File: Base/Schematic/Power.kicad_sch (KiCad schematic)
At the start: 13 parts, among them U2 TPS560430XDBV

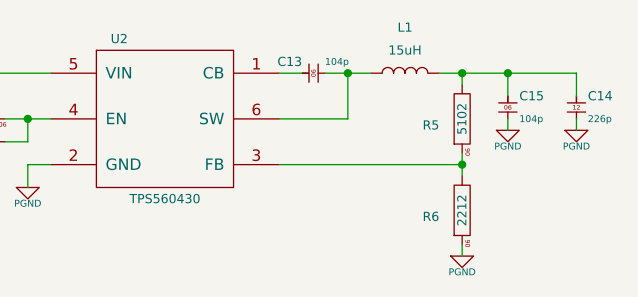
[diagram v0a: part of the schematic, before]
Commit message: [BOM 문서 테스트] - Libreoffice로 BOM 문서 출력 테스트 - 회로도에 CAN transceiver 추가
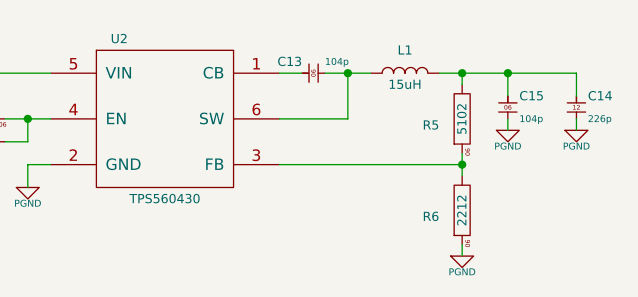
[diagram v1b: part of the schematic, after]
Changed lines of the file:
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@@
 		(on_board yes)
 		(dnp no)
-		(fields_autoplaced yes)
 		(property "Reference" "L1"
-			(at 176.53 92.71 0)
+			(at 176.53 95.25 0)
 			(effects
 				(font
@@
 		)
 		(property "#Value" "15uH"
-			(at 176.53 95.25 0)
+			(at 176.53 99.06 0)
 			(effects
 				(font

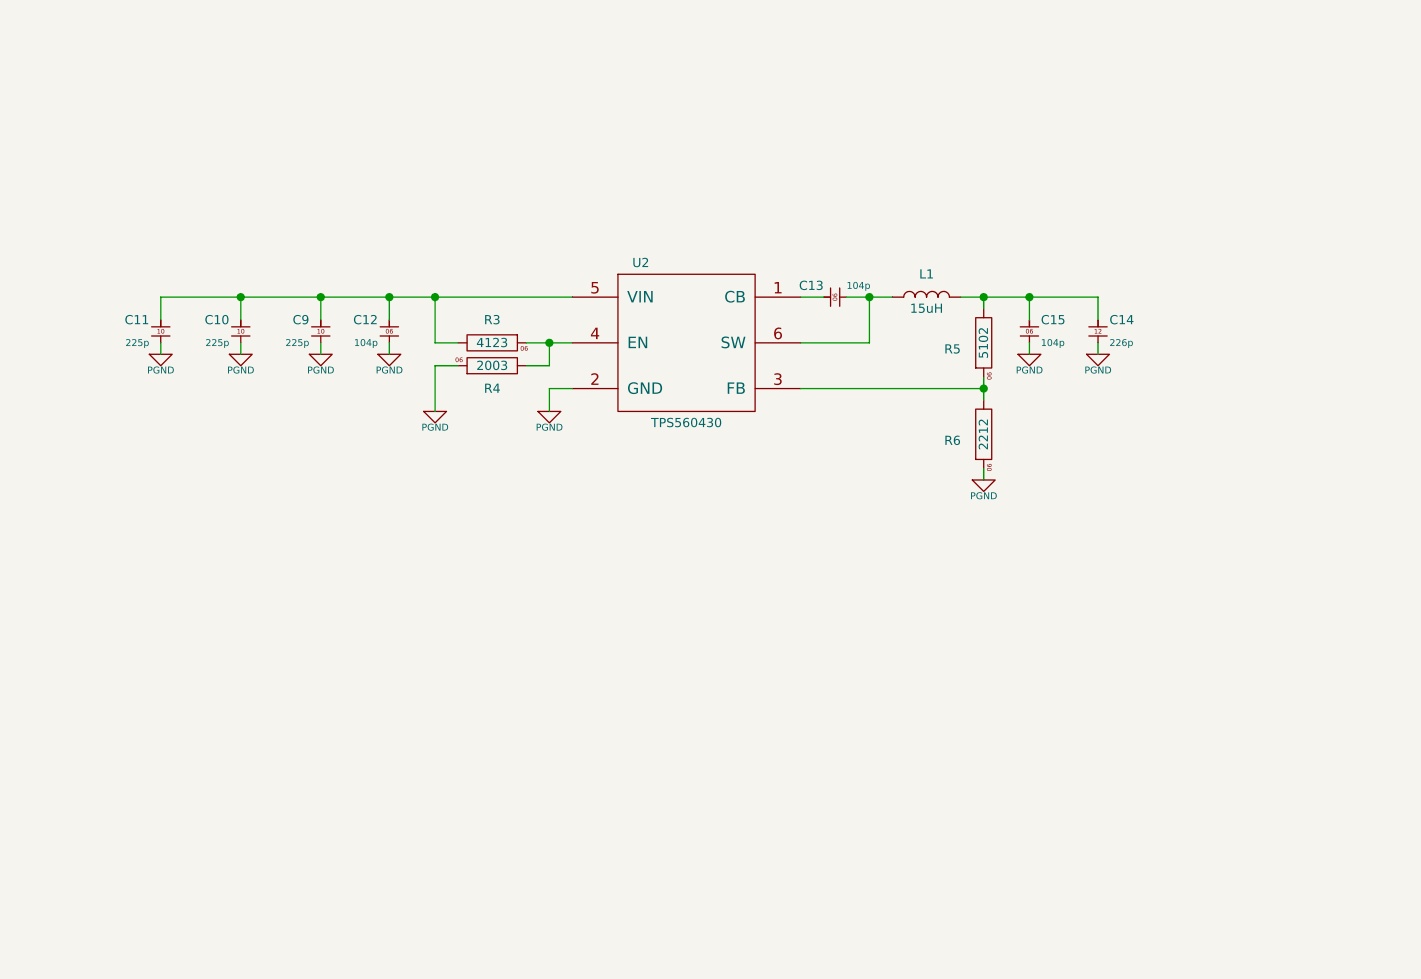
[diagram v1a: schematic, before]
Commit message: [Base 회로도 업데이트] - 5V 전원 추가 - 3.3V, 5V 회로도 보완
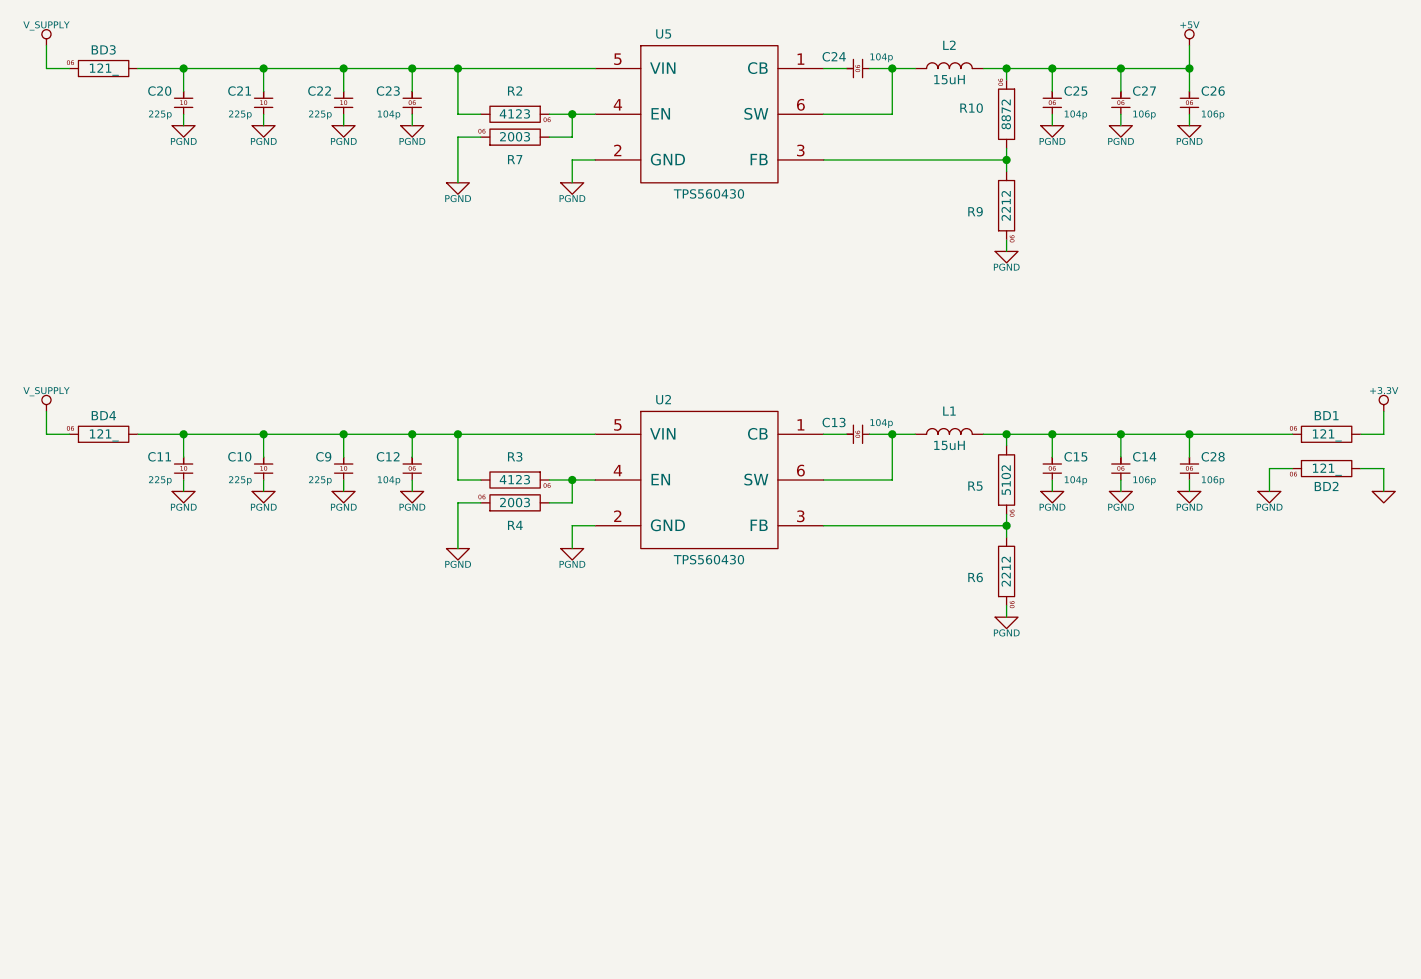
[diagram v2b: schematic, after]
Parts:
- removed C14: 1206B226K100, SMC:1206, symbol Capacitor_MLCC:1206B226K100
- added BD1, BD2, BD3, BD4: BLM18KG121TN1D, SML:0603, symbol BEAD:BLM18KG121TN1D
- added C14, C26, C27, C28: 0603X106K100, SMC:0603, symbol Capacitor_MLCC:0603X106K100
- added C20, C21, C22: 1210B225K101, SMC:1210, symbol Capacitor_MLCC:1210B225K101
- added C23, C24, C25: 0603B104K500, SMC:0603, symbol Capacitor_MLCC:0603B104K500
- added L2: SWPA5040S150MT, Sunlord:SWPA5040S, symbol Inductor_Power:SWPA5040S150MT
- added R10: WR06X8872FTL, SMR:0603, symbol Resistor:WR06X8872FTL
- added R2: WR06X4123FTL, SMR:0603, symbol Resistor:WR06X4123FTL
- added R7: WR06X2003FTL, SMR:0603, symbol Resistor:WR06X2003FTL
- added R9: WR06X2212FTL, SMR:0603, symbol Resistor:WR06X2212FTL
- added U5: TPS560430XDBV, TI:DBV0006A, symbol Power_DCDC:TPS560430XDBV
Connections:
- net PGND: now also BD2.1, C14.1, C20.1, C21.1, C22.1, C23.1, C25.1, C26.1, C27.1, C28.1, R7.1, R9.1, U5.2 (GND)
- net at C15.2, L1.2, R5.2: now also BD1.1, C14.2, C28.2
- net at C10.2, C11.2, C12.2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: now also BD4.2
- new net: BD3.2, C20.2, C21.2, C22.2, C23.2, R2.2, U5.5 (VIN)
- new net: R10.2, R9.2, U5.3 (FB)
- new net: C24.1, L2.1, U5.6 (SW)
- new net: C24.2, U5.1 (CB)
- new net: R2.1, R7.2, U5.4 (EN)
- new net +3.3V: BD1.2
- new net +5V: C25.2, C26.2, C27.2, L2.2, R10.1
- new net GND: BD2.2
- new net V_SUPPLY: BD3.1, BD4.1
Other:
- moved on the sheet: C10, C11, C12, C13, C15, C9, L1, R3, R4, R5, R6, U2

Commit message: [Base PCB 업데이트] - PCB 외곽선과 볼트 위치 설정
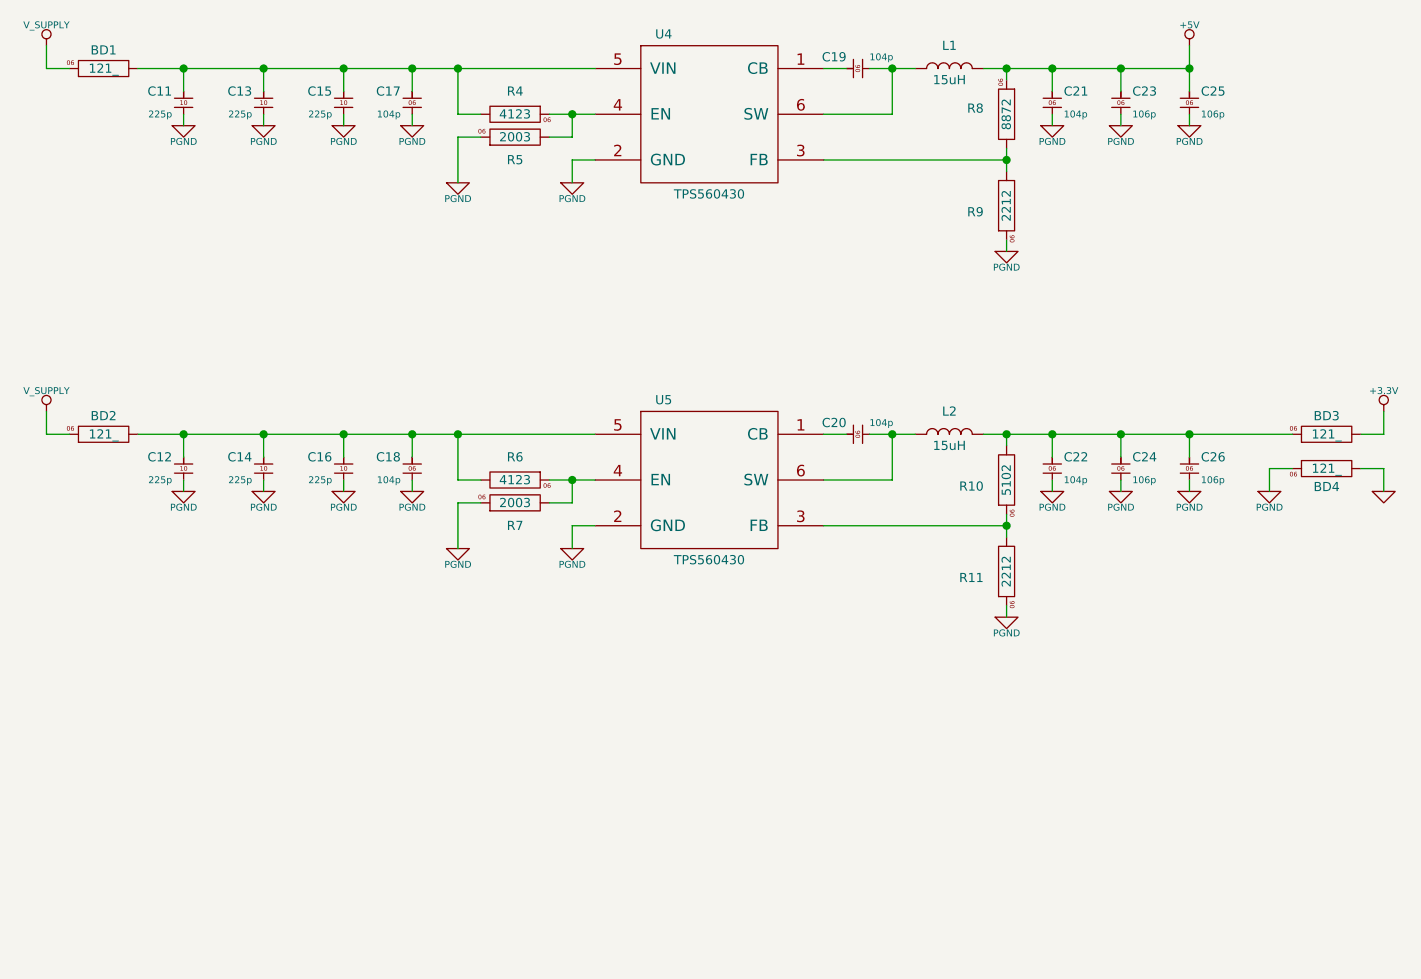
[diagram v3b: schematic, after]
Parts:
- renumbered BD3 to BD1, BD4 to BD2, BD1 to BD3, BD2 to BD4, C20 to C11, C11 to C12, C21 to C13, C10 to C14, C22 to C15, C9 to C16, C23 to C17, C12 to C18, C24 to C19, C13 to C20, C25 to C21, C15 to C22, C27 to C23, C14 to C24, C26 to C25, C28 to C26, L2 to L1, L1 to L2, R5 to R10, R6 to R11, R2 to R4, R7 to R5, R3 to R6, R4 to R7, R10 to R8, U5 to U4, U2 to U5

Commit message: [Base 회로도 업데이트] - AIN 입력 4개 추가
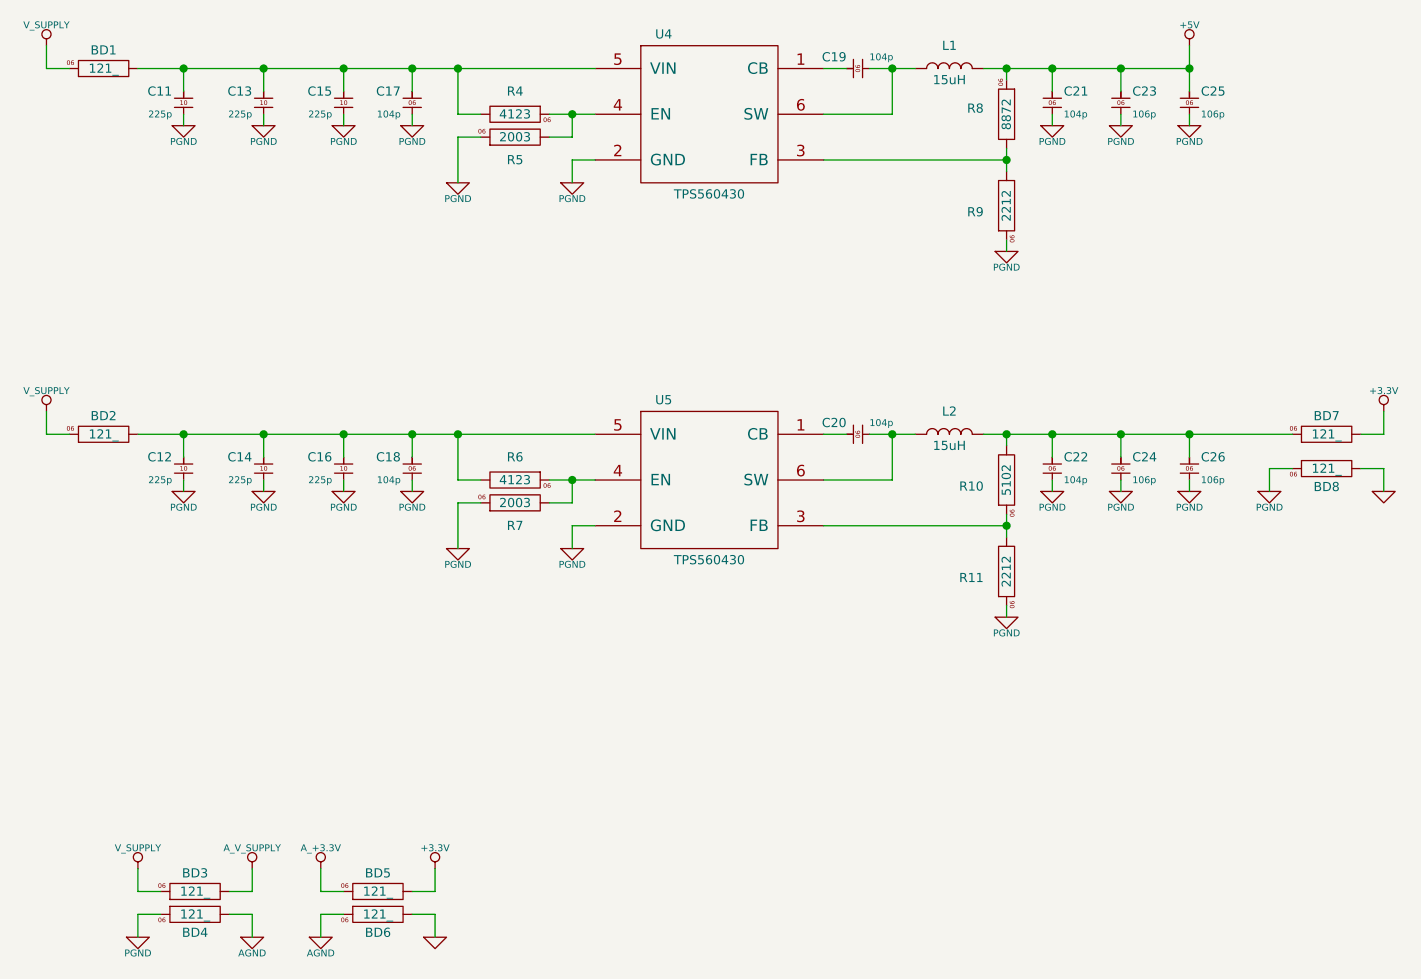
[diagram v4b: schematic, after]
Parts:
- added BD3, BD4, BD5, BD6: BLM18KG121TN1D, SML:0603, symbol BEAD:BLM18KG121TN1D
- renumbered BD3 to BD7, BD4 to BD8
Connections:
- net +3.3V: now also BD5.2
- net GND: now also BD6.2
- net PGND: now also BD4.1
- net V_SUPPLY: now also BD3.1
- new net AGND: BD4.2, BD6.1
- new net A_+3.3V: BD5.1
- new net A_V_SUPPLY: BD3.2
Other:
- company: (none) -> -
- title: (none) -> Open-PLC-Project
